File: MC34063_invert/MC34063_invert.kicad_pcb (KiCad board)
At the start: 2 copper layers, 88.6 x 24 mm, 23 parts, among them J1 INPUT, J2 OUTPUT, Q1 BC557, U1 MC34063AP

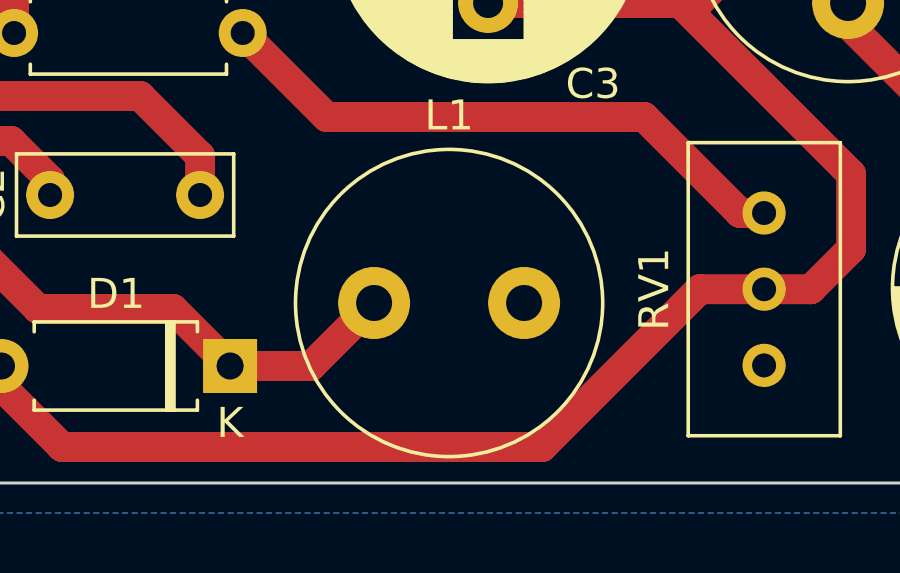
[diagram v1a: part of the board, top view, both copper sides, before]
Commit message: Fixed error in feedback loop
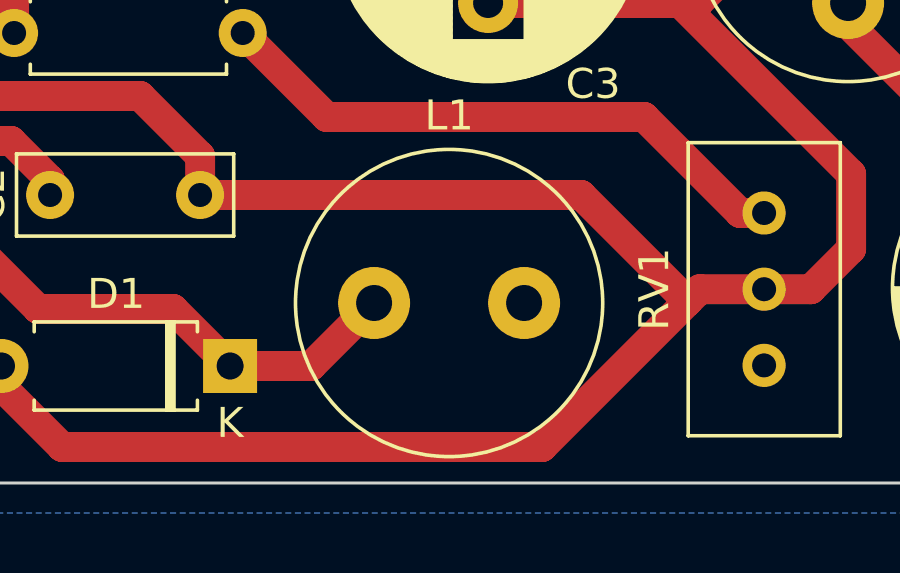
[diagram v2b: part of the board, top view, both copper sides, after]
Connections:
- C3 pad 2: Net-(C3-Pad2) -> Net-(C2-Pad2)
- D1 pad 2: Net-(C3-Pad2) -> Net-(C2-Pad2)
- L2 pad 1: Net-(C3-Pad2) -> Net-(C2-Pad2)
- RV1 pad 2: Net-(C3-Pad2) -> Net-(C2-Pad2)
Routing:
- net Net-(C2-Pad2): track 13.6 -> 88.5 mm
- net Net-(C3-Pad2): track 57.2 -> 0.00 mm

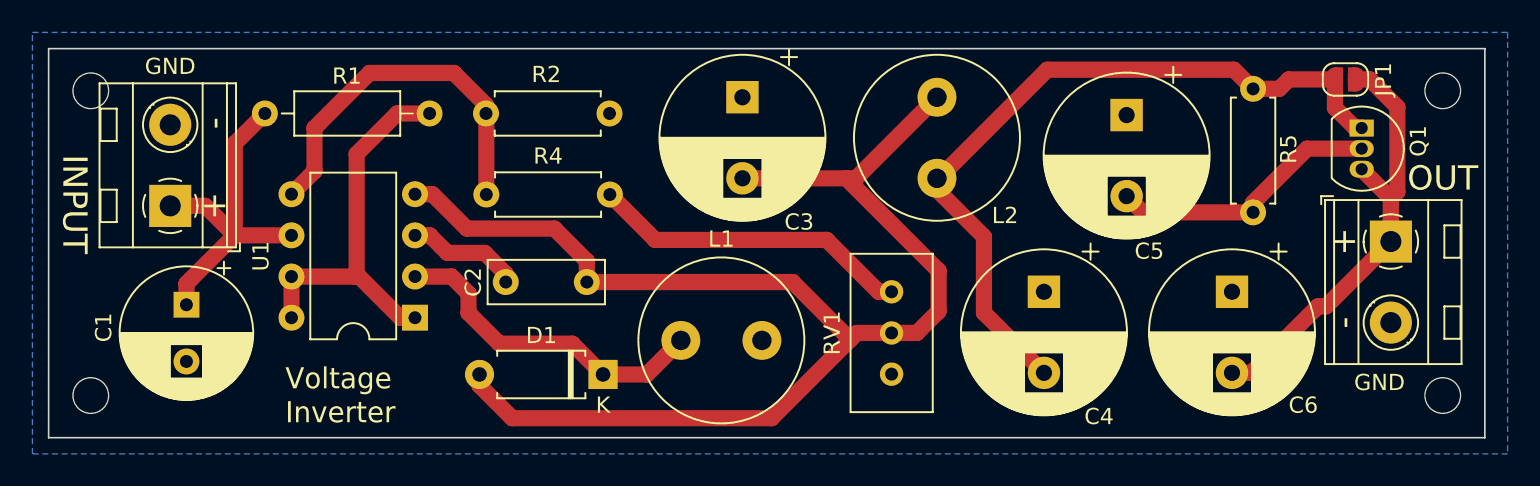
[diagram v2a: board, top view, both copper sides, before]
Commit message: Made buck & inverter PCB's smaller for panelization
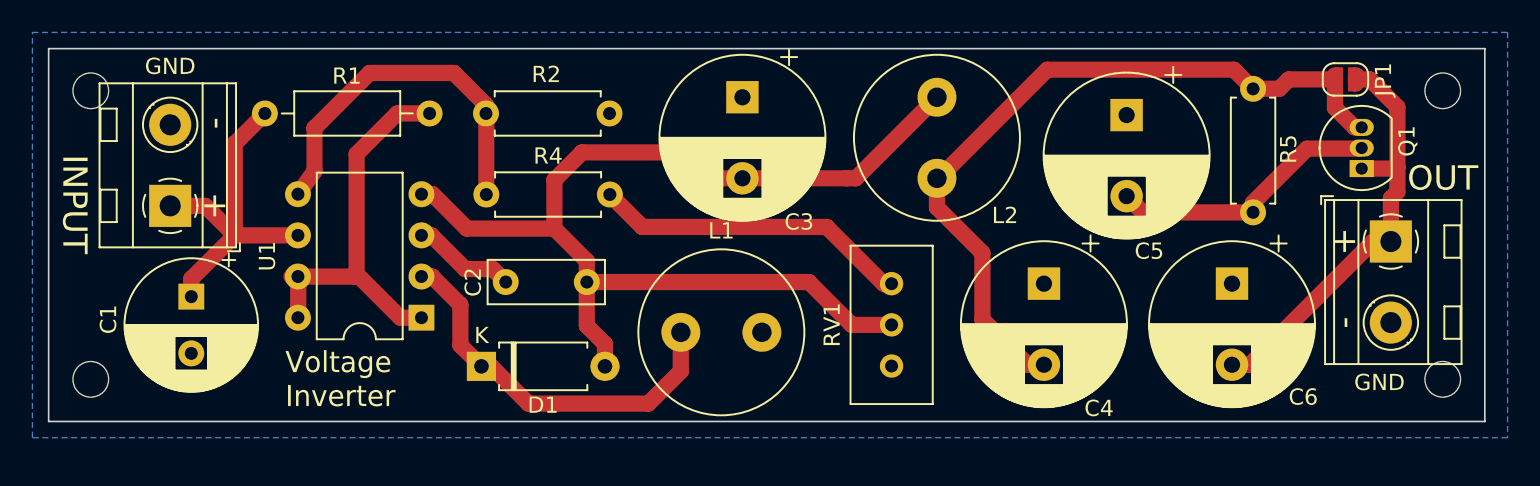
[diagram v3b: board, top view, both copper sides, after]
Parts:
- Q1: value BC557 -> 2N2907
- moved D1 7.52 mm to (71.7, 78.6), turned to 0 degrees
- moved Q1 2.50 mm to (126.0, 66.4), turned to 90 degrees
- moved H1 1.00 mm to (47.6, 79.4)
- moved H4 1.00 mm to (131.0, 79.4)
- moved C1 0.58 mm to (53.8, 74.3)
- moved C4 0.50 mm to (106.4, 73.5)
- moved C6 0.50 mm to (118.0, 73.5)
- moved L1 0.50 mm to (84.0, 76.5)
- moved RV1 0.50 mm to (97.0, 73.5)
- moved U1 0.40 mm to (68.0, 75.6)
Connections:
- Q1 pad 1: Net-(C4-Pad2) -> Net-(C6-Pad2)
- Q1 pad 3: Net-(C6-Pad2) -> Net-(C4-Pad2)
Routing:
- net Net-(C2-Pad2): track 88.5 -> 68.8 mm
- net Net-(D1-Pad1): track 20.5 -> 23.9 mm
- net Net-(C2-Pad1): track 7.09 -> 6.39 mm
- net Net-(C6-Pad2): track 27.4 -> 26.9 mm
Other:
- board size 88.6 x 24 mm -> 88.6 x 23 mm
